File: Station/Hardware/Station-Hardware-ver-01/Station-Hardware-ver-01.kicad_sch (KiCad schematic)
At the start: 28 parts, among them J1 Barrel_Jack, J2 Conn_01x03_Male, J3 Conn_01x03_Male, J4 4P4C, J5 4P4C, J6 Conn_01x03_Male, U1 YAAJ_BluePill, U2 DS3231_Full_Pinout, U3 SX1278_Minimal, U4 MCP6002-xP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

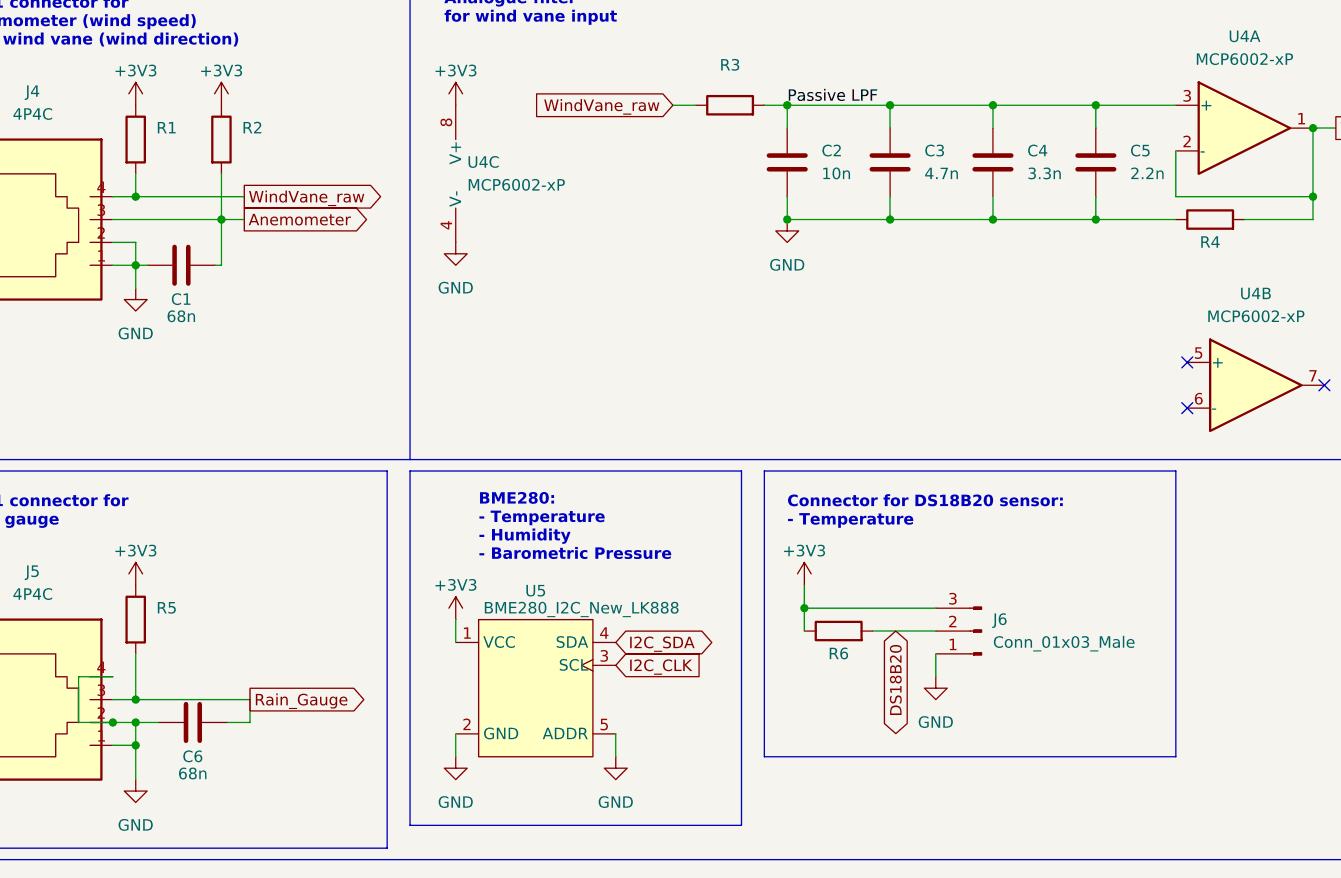
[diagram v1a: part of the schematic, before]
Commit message: station pcb: update ceramic capacitors to smd
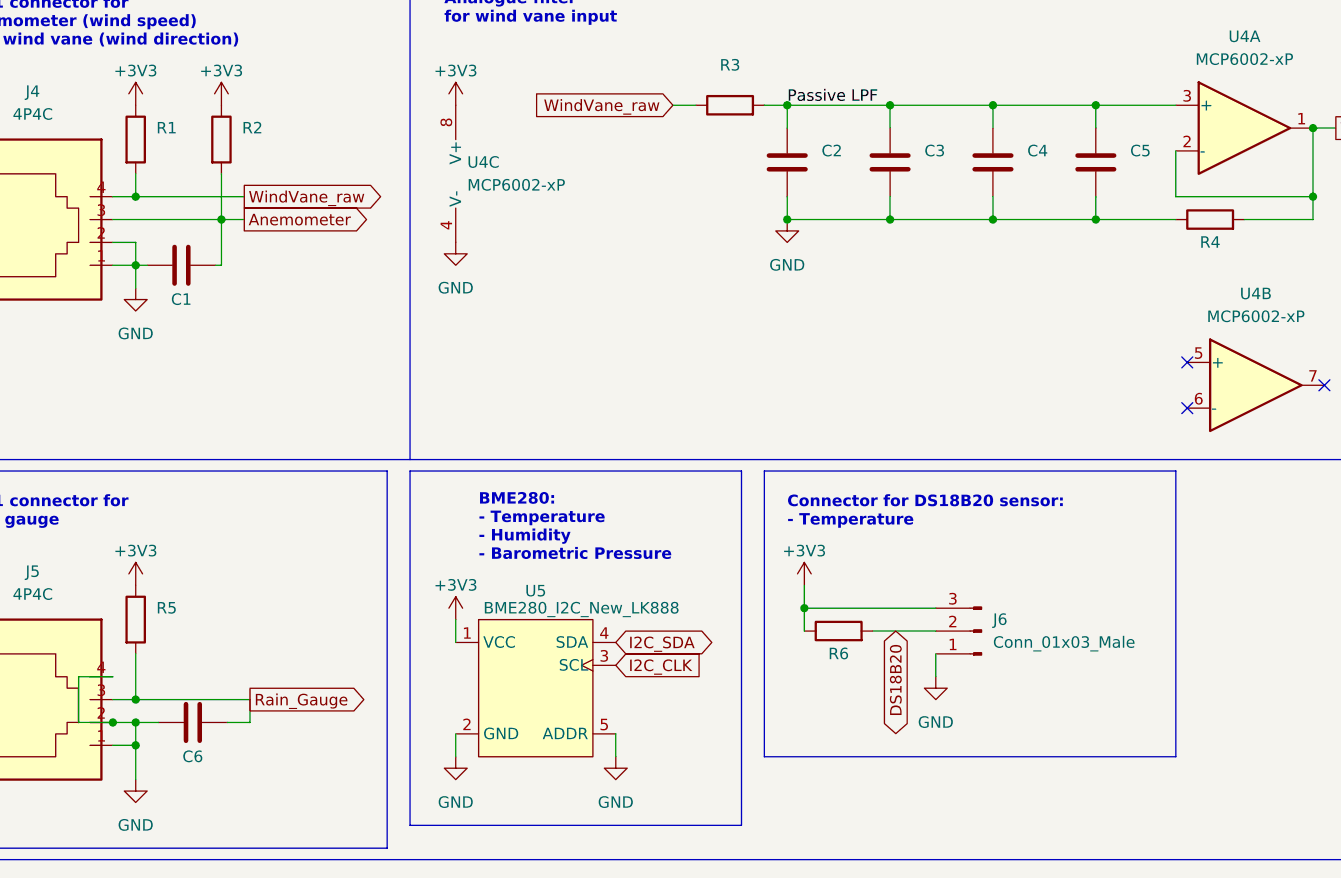
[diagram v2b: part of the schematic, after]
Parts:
- C1, C6: value 68n -> (none); footprint Capacitor_THT:C_Disc_D8.0mm_W5.0mm_P7.50mm -> (none)
- C2: value 10n -> (none); footprint Capacitor_THT:C_Disc_D5.1mm_W3.2mm_P5.00mm -> (none)
- C3: value 4.7n -> (none); footprint Capacitor_THT:C_Disc_D5.1mm_W3.2mm_P5.00mm -> (none)
- C4: value 3.3n -> (none); footprint Capacitor_THT:C_Disc_D5.1mm_W3.2mm_P5.00mm -> (none)
- C5: value 2.2n -> (none); footprint Capacitor_THT:C_Disc_D5.1mm_W3.2mm_P5.00mm -> (none)
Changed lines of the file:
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@@
     (in_bom yes) (on_board yes)
     (property "Reference" "C1" (id 0) (at 127 101.6 90))
-    (property "Value" "68n" (id 1) (at 127 103.505 90))
-    (property "Footprint" "Capacitor_THT:C_Disc_D8.0mm_W5.0mm_P7.50mm" (id 2) (at 130.81 96.8248 0)
+    (property "Value" "" (id 1) (at 127 103.505 90))
+    (property "Footprint" "" (id 2) (at 130.81 96.8248 0)
       (effects (font (size 1.27 1.27)) hide)
     )
@@
       (effects (font (size 1.27 1.27)) (justify left))
     )
-    (property "Value" "10n" (id 1) (at 198.12 87.6299 0)
-      (effects (font (size 1.27 1.27)) (justify left))
-    )
-    (property "Footprint" "Capacitor_THT:C_Disc_D5.1mm_W3.2mm_P5.00mm" (id 2) (at 195.2752 90.17 0)
+    (property "Value" "" (id 1) (at 198.12 87.6299 0)
+      (effects (font (size 1.27 1.27)) (justify left))
+    )
+    (property "Footprint" "" (id 2) (at 195.2752 90.17 0)
       (effects (font (size 1.27 1.27)) hide)
     )
@@
       (effects (font (size 1.27 1.27)) (justify left))
     )
-    (property "Value" "4.7n" (id 1) (at 209.55 87.6299 0)
-      (effects (font (size 1.27 1.27)) (justify left))
-    )
-    (property "Footprint" "Capacitor_THT:C_Disc_D5.1mm_W3.2mm_P5.00mm" (id 2) (at 206.7052 90.17 0)
+    (property "Value" "" (id 1) (at 209.55 87.6299 0)
+      (effects (font (size 1.27 1.27)) (justify left))
+    )
+    (property "Footprint" "" (id 2) (at 206.7052 90.17 0)
       (effects (font (size 1.27 1.27)) hide)
     )
@@
       (effects (font (size 1.27 1.27)) (justify left))
     )
-    (property "Value" "2.2n" (id 1) (at 232.41 87.6299 0)
-      (effects (font (size 1.27 1.27)) (justify left))
-    )
-    (property "Footprint" "Capacitor_THT:C_Disc_D5.1mm_W3.2mm_P5.00mm" (id 2) (at 229.5652 90.17 0)
+    (property "Value" "" (id 1) (at 232.41 87.6299 0)
+      (effects (font (size 1.27 1.27)) (justify left))
+    )
+    (property "Footprint" "" (id 2) (at 229.5652 90.17 0)
       (effects (font (size 1.27 1.27)) hide)
     )
@@
     (in_bom yes) (on_board yes)
     (property "Reference" "C6" (id 0) (at 128.27 152.4 90))
-    (property "Value" "68n" (id 1) (at 128.27 154.305 90))
-    (property "Footprint" "Capacitor_THT:C_Disc_D8.0mm_W5.0mm_P7.50mm" (id 2) (at 132.08 147.6248 0)
+    (property "Value" "" (id 1) (at 128.27 154.305 90))
+    (property "Footprint" "" (id 2) (at 132.08 147.6248 0)
       (effects (font (size 1.27 1.27)) hide)
     )
@@
       (effects (font (size 1.27 1.27)) (justify left))
     )
-    (property "Value" "3.3n" (id 1) (at 220.98 87.6299 0)
-      (effects (font (size 1.27 1.27)) (justify left))
-    )
-    (property "Footprint" "Capacitor_THT:C_Disc_D5.1mm_W3.2mm_P5.00mm" (id 2) (at 218.1352 90.17 0)
+    (property "Value" "" (id 1) (at 220.98 87.6299 0)
+      (effects (font (size 1.27 1.27)) (justify left))
+    )
+    (property "Footprint" "" (id 2) (at 218.1352 90.17 0)
       (effects (font (size 1.27 1.27)) hide)
     )
@@
     )
     (path "/2449ad7e-7c10-430f-8adf-47601bb4af79"
-      (reference "C1") (unit 1) (value "68n") (footprint "Capacitor_THT:C_Disc_D8.0mm_W5.0mm_P7.50mm")
+      (reference "C1") (unit 1) (value "68n") (footprint "Capacitor_SMD:C_0805_2012Metric_Pad1.18x1.45mm_HandSolder")
     )
     (path "/5205aebd-9933-4ae9-a0ce-7844b2f8a68d"
-      (reference "C2") (unit 1) (value "10n") (footprint "Capacitor_THT:C_Disc_D5.1mm_W3.2mm_P5.00mm")
+      (reference "C2") (unit 1) (value "10n") (footprint "Capacitor_SMD:C_0805_2012Metric_Pad1.18x1.45mm_HandSolder")
     )
     (path "/7b4ce615-f0d5-4b1f-9b49-d02fdef0cf8b"
-      (reference "C3") (unit 1) (value "4.7n") (footprint "Capacitor_THT:C_Disc_D5.1mm_W3.2mm_P5.00mm")
+      (reference "C3") (unit 1) (value "4.7n") (footprint "Capacitor_SMD:C_0805_2012Metric_Pad1.18x1.45mm_HandSolder")
     )
     (path "/ee8bc577-8a80-4c3d-a67d-e6eec779095a"
-      (reference "C4") (unit 1) (value "3.3n") (footprint "Capacitor_THT:C_Disc_D5.1mm_W3.2mm_P5.00mm")
+      (reference "C4") (unit 1) (value "3.3n") (footprint "Capacitor_SMD:C_0805_2012Metric_Pad1.18x1.45mm_HandSolder")
     )
     (path "/b2222e6a-882c-40d4-b385-6d8027e3c680"
-      (reference "C5") (unit 1) (value "2.2n") (footprint "Capacitor_THT:C_Disc_D5.1mm_W3.2mm_P5.00mm")
+      (reference "C5") (unit 1) (value "2.2n") (footprint "Capacitor_SMD:C_0805_2012Metric_Pad1.18x1.45mm_HandSolder")
     )
     (path "/e3ba159d-1c8d-4463-8593-7c4527b943a6"
-      (reference "C6") (unit 1) (value "68n") (footprint "Capacitor_THT:C_Disc_D8.0mm_W5.0mm_P7.50mm")
+      (reference "C6") (unit 1) (value "68n") (footprint "Capacitor_SMD:C_0805_2012Metric_Pad1.18x1.45mm_HandSolder")
     )
     (path "/2c419f21-4de9-4e15-9e60-5df2ad3dae9f"

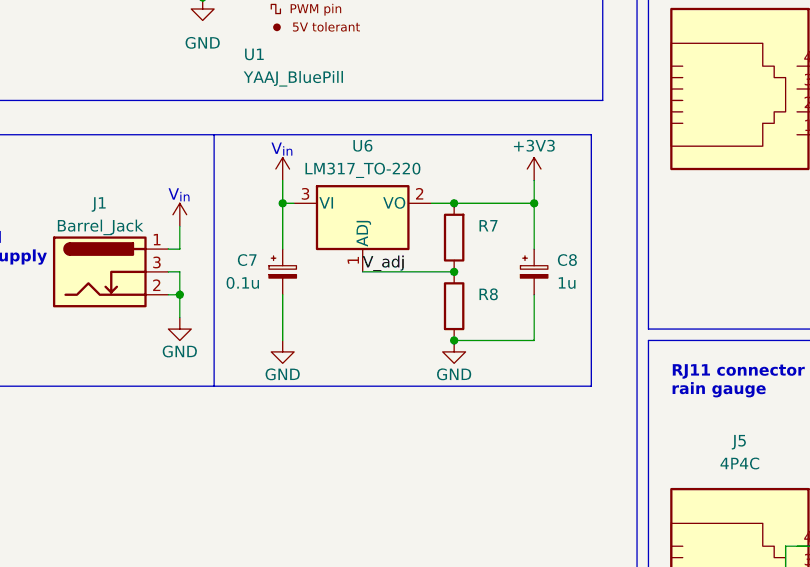
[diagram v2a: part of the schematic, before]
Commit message: station pcb: update electrolytic capacitors to smd
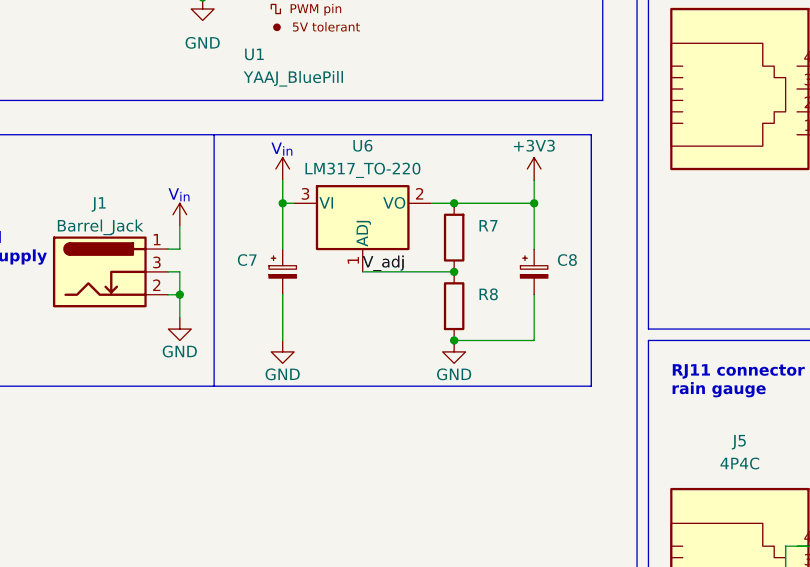
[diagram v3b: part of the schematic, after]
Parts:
- C7: value 0.1u -> (none); footprint Capacitor_THT:CP_Radial_D5.0mm_P2.00mm -> (none)
- C8: value 1u -> (none); footprint Capacitor_THT:CP_Radial_D5.0mm_P2.00mm -> (none)
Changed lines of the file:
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@@
       (effects (font (size 1.27 1.27)) (justify left))
     )
-    (property "Value" "0.1u" (id 1) (at 53.34 114.3 0)
-      (effects (font (size 1.27 1.27)) (justify left))
-    )
-    (property "Footprint" "Capacitor_THT:CP_Radial_D5.0mm_P2.00mm" (id 2) (at 59.69 113.03 0)
+    (property "Value" "" (id 1) (at 53.34 114.3 0)
+      (effects (font (size 1.27 1.27)) (justify left))
+    )
+    (property "Footprint" "" (id 2) (at 59.69 113.03 0)
       (effects (font (size 1.27 1.27)) hide)
     )
@@
       (effects (font (size 1.27 1.27)) (justify left))
     )
-    (property "Value" "1u" (id 1) (at 90.17 114.3 0)
-      (effects (font (size 1.27 1.27)) (justify left))
-    )
-    (property "Footprint" "Capacitor_THT:CP_Radial_D5.0mm_P2.00mm" (id 2) (at 87.63 113.03 0)
+    (property "Value" "" (id 1) (at 90.17 114.3 0)
+      (effects (font (size 1.27 1.27)) (justify left))
+    )
+    (property "Footprint" "" (id 2) (at 87.63 113.03 0)
       (effects (font (size 1.27 1.27)) hide)
     )
@@
     )
     (path "/2c419f21-4de9-4e15-9e60-5df2ad3dae9f"
-      (reference "C7") (unit 1) (value "0.1u") (footprint "Capacitor_THT:CP_Radial_D5.0mm_P2.00mm")
+      (reference "C7") (unit 1) (value "0.1u") (footprint "Capacitor_SMD:CP_Elec_4x5.4")
     )
     (path "/3563f528-c66a-48e6-8a05-9c7fa879b89e"
-      (reference "C8") (unit 1) (value "1u") (footprint "Capacitor_THT:CP_Radial_D5.0mm_P2.00mm")
+      (reference "C8") (unit 1) (value "1u") (footprint "Capacitor_SMD:CP_Elec_4x5.4")
     )
     (path "/ca273977-daf6-4d89-84c3-215dd45177c9"

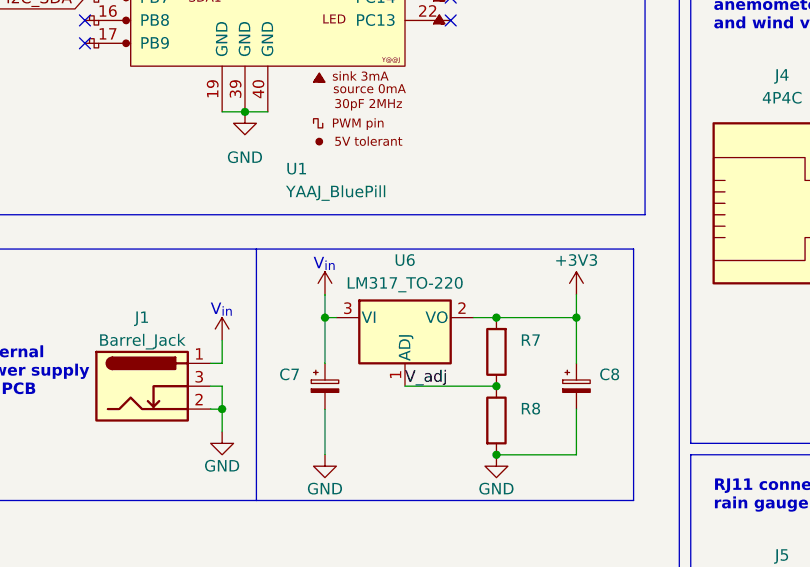
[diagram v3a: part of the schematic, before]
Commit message: station pcb: change LM317 footprint
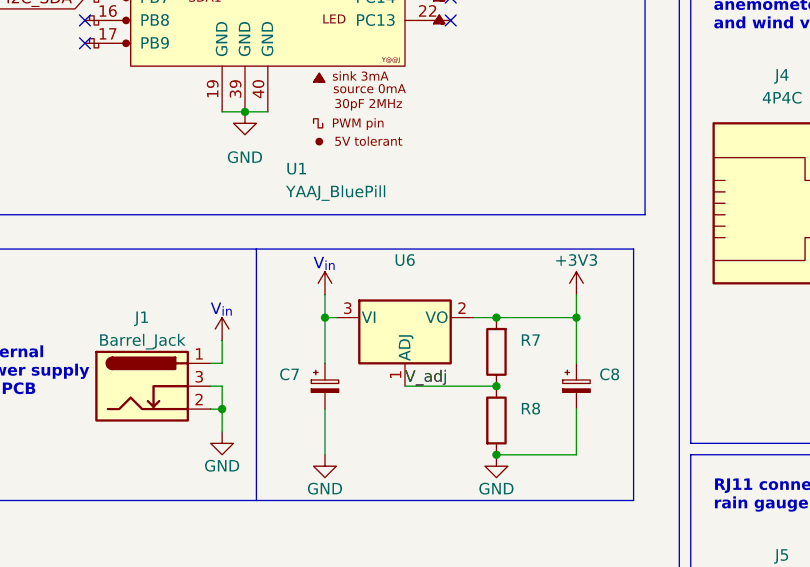
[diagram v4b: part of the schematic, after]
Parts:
- U6: value LM317_TO-220 -> (none); footprint Package_TO_SOT_THT:TO-220-3_Vertical -> (none)
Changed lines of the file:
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@@
     (in_bom yes) (on_board yes)
     (property "Reference" "U6" (id 0) (at 68.58 99.06 0))
-    (property "Value" "LM317_TO-220" (id 1) (at 68.58 101.6 0))
-    (property "Footprint" "Package_TO_SOT_THT:TO-220-3_Vertical" (id 2) (at 68.58 99.06 0)
+    (property "Value" "" (id 1) (at 68.58 101.6 0))
+    (property "Footprint" "" (id 2) (at 68.58 99.06 0)
       (effects (font (size 1.27 1.27) italic) hide)
     )
@@
     )
     (path "/77006be8-e871-4875-98bd-df9b9f9c71da"
-      (reference "U6") (unit 1) (value "LM317_TO-220") (footprint "Package_TO_SOT_THT:TO-220-3_Vertical")
-    )
-  )
+      (reference "U6") (unit 1) (value "LM317_TO-220") (footprint "Package_TO_SOT_THT:TO-220-3_Horizontal_TabDown")
+    )
+  )
